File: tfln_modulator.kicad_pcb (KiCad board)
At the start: 4 copper layers, 60 x 40 mm, 9 parts

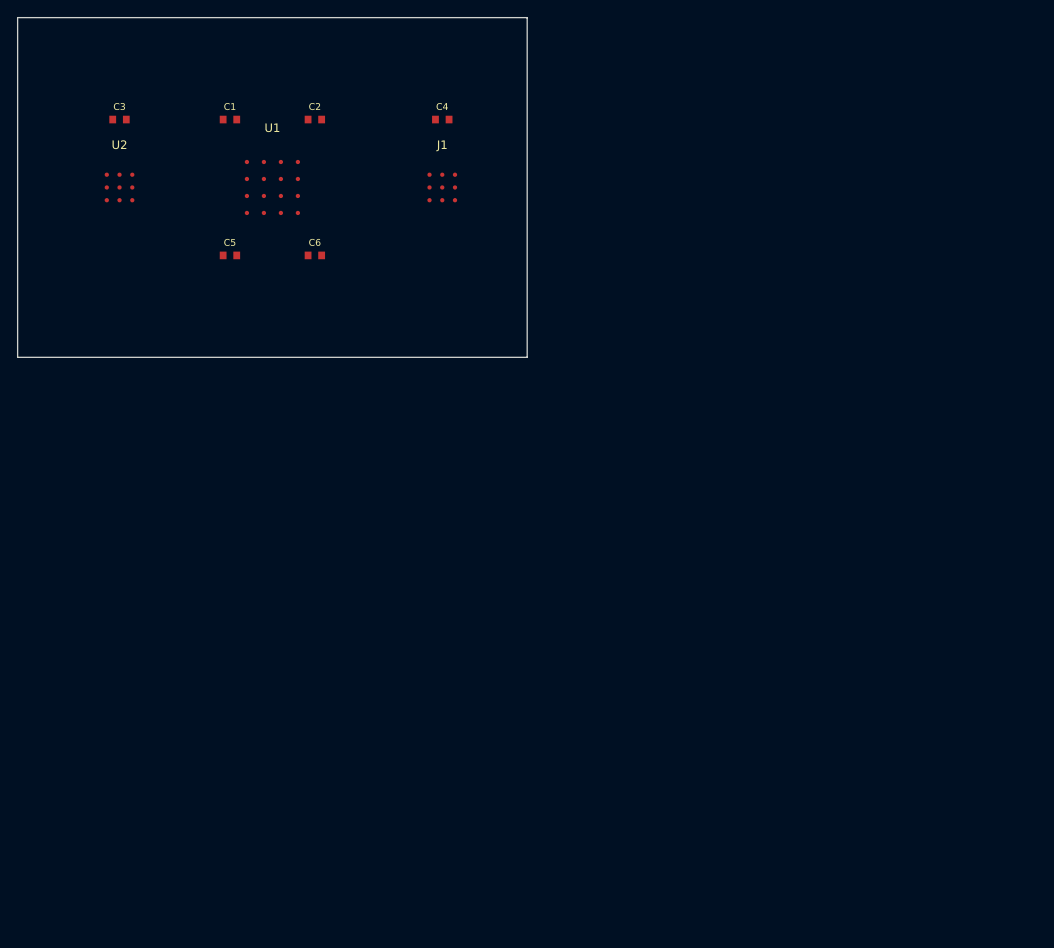
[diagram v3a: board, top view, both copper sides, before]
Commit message: Ultra high-density PCB: 634 nets, 600+ components, TFLN-AI Core + HBM + VRM
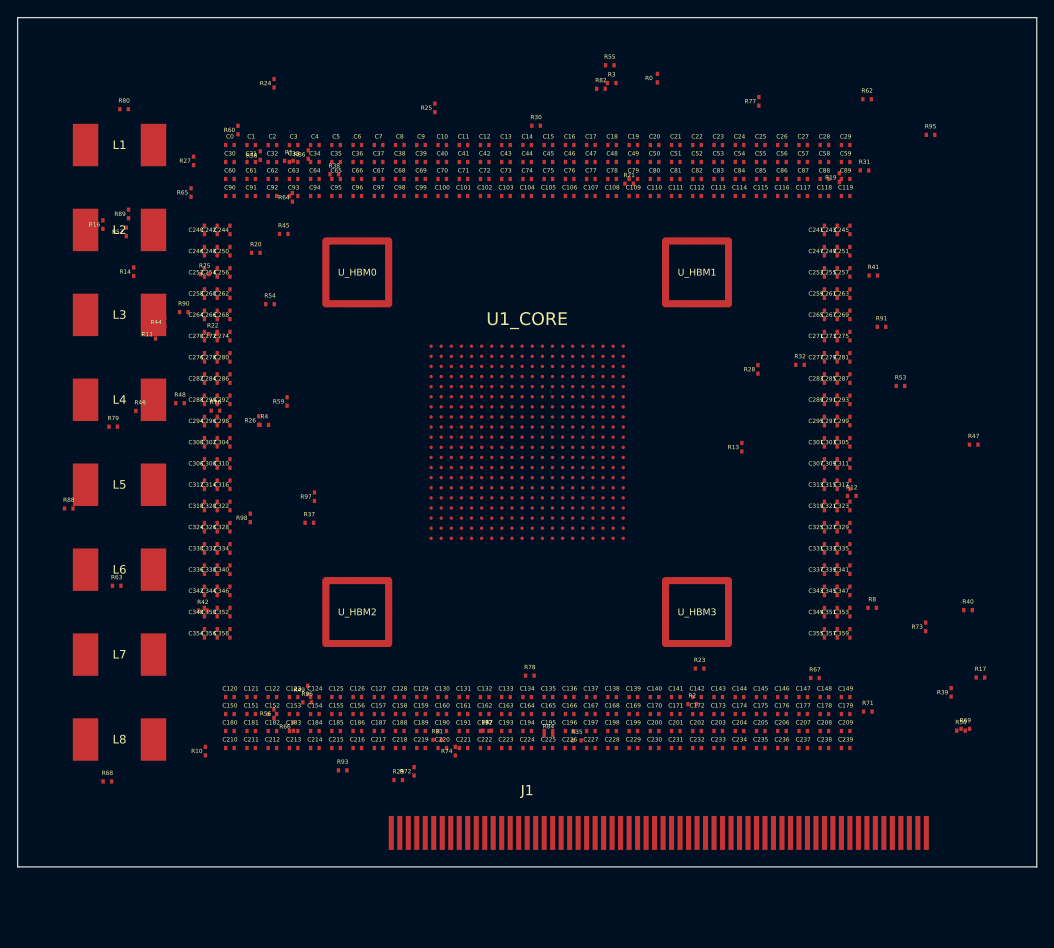
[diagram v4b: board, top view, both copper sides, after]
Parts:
- removed U1: , Custom:U1
- removed U2: , Custom:U2
- added C0: , SMD:0402, F.Cu at (25.0, 15.0)
- added C10: , SMD:0402, F.Cu at (50.0, 15.0)
- added C100: , SMD:0402, F.Cu at (50.0, 21.0)
- added C101: , SMD:0402, F.Cu at (52.5, 21.0)
- added C102: , SMD:0402, F.Cu at (55.0, 21.0)
- added C103: , SMD:0402, F.Cu at (57.5, 21.0)
- added C104: , SMD:0402, F.Cu at (60.0, 21.0)
- added C105: , SMD:0402, F.Cu at (62.5, 21.0)
- added C106: , SMD:0402, F.Cu at (65.0, 21.0)
- added C107: , SMD:0402, F.Cu at (67.5, 21.0)
- added C108: , SMD:0402, F.Cu at (70.0, 21.0)
- added C109: , SMD:0402, F.Cu at (72.5, 21.0)
- added C11: , SMD:0402, F.Cu at (52.5, 15.0)
- added C110: , SMD:0402, F.Cu at (75.0, 21.0)
- added C111: , SMD:0402, F.Cu at (77.5, 21.0)
- added C112: , SMD:0402, F.Cu at (80.0, 21.0)
- added C113: , SMD:0402, F.Cu at (82.5, 21.0)
- added C114: , SMD:0402, F.Cu at (85.0, 21.0)
- added C115: , SMD:0402, F.Cu at (87.5, 21.0)
- added C116: , SMD:0402, F.Cu at (90.0, 21.0)
- added C117: , SMD:0402, F.Cu at (92.5, 21.0)
- added C118: , SMD:0402, F.Cu at (95.0, 21.0)
- added C119: , SMD:0402, F.Cu at (97.5, 21.0)
- added C12: , SMD:0402, F.Cu at (55.0, 15.0)
- added C120: , SMD:0402, F.Cu at (25.0, 80.0)
- added C121: , SMD:0402, F.Cu at (27.5, 80.0)
- added C122: , SMD:0402, F.Cu at (30.0, 80.0)
- added C123: , SMD:0402, F.Cu at (32.5, 80.0)
- added C124: , SMD:0402, F.Cu at (35.0, 80.0)
- added C125: , SMD:0402, F.Cu at (37.5, 80.0)
- added C126: , SMD:0402, F.Cu at (40.0, 80.0)
- added C127: , SMD:0402, F.Cu at (42.5, 80.0)
- added C128: , SMD:0402, F.Cu at (45.0, 80.0)
- added C129: , SMD:0402, F.Cu at (47.5, 80.0)
- added C13: , SMD:0402, F.Cu at (57.5, 15.0)
- added C130: , SMD:0402, F.Cu at (50.0, 80.0)
- added C131: , SMD:0402, F.Cu at (52.5, 80.0)
- added C132: , SMD:0402, F.Cu at (55.0, 80.0)
- added C133: , SMD:0402, F.Cu at (57.5, 80.0)
- added C134: , SMD:0402, F.Cu at (60.0, 80.0)
- added C135: , SMD:0402, F.Cu at (62.5, 80.0)
- added C136: , SMD:0402, F.Cu at (65.0, 80.0)
- added C137: , SMD:0402, F.Cu at (67.5, 80.0)
- added C138: , SMD:0402, F.Cu at (70.0, 80.0)
- added C139: , SMD:0402, F.Cu at (72.5, 80.0)
- added C14: , SMD:0402, F.Cu at (60.0, 15.0)
- added C140: , SMD:0402, F.Cu at (75.0, 80.0)
- added C141: , SMD:0402, F.Cu at (77.5, 80.0)
- added C142: , SMD:0402, F.Cu at (80.0, 80.0)
- added C143: , SMD:0402, F.Cu at (82.5, 80.0)
- added C144: , SMD:0402, F.Cu at (85.0, 80.0)
- added C145: , SMD:0402, F.Cu at (87.5, 80.0)
- added C146: , SMD:0402, F.Cu at (90.0, 80.0)
- added C147: , SMD:0402, F.Cu at (92.5, 80.0)
- added C148: , SMD:0402, F.Cu at (95.0, 80.0)
- added C149: , SMD:0402, F.Cu at (97.5, 80.0)
- added C15: , SMD:0402, F.Cu at (62.5, 15.0)
- added C150: , SMD:0402, F.Cu at (25.0, 82.0)
- added C151: , SMD:0402, F.Cu at (27.5, 82.0)
- added C152: , SMD:0402, F.Cu at (30.0, 82.0)
- added C153: , SMD:0402, F.Cu at (32.5, 82.0)
- added C154: , SMD:0402, F.Cu at (35.0, 82.0)
- added C155: , SMD:0402, F.Cu at (37.5, 82.0)
- added C156: , SMD:0402, F.Cu at (40.0, 82.0)
- added C157: , SMD:0402, F.Cu at (42.5, 82.0)
- added C158: , SMD:0402, F.Cu at (45.0, 82.0)
- added C159: , SMD:0402, F.Cu at (47.5, 82.0)
- added C16: , SMD:0402, F.Cu at (65.0, 15.0)
- added C160: , SMD:0402, F.Cu at (50.0, 82.0)
- added C161: , SMD:0402, F.Cu at (52.5, 82.0)
- added C162: , SMD:0402, F.Cu at (55.0, 82.0)
- added C163: , SMD:0402, F.Cu at (57.5, 82.0)
- added C164: , SMD:0402, F.Cu at (60.0, 82.0)
- added C165: , SMD:0402, F.Cu at (62.5, 82.0)
- added C166: , SMD:0402, F.Cu at (65.0, 82.0)
- added C167: , SMD:0402, F.Cu at (67.5, 82.0)
- added C168: , SMD:0402, F.Cu at (70.0, 82.0)
- added C169: , SMD:0402, F.Cu at (72.5, 82.0)
- added C17: , SMD:0402, F.Cu at (67.5, 15.0)
- added C170: , SMD:0402, F.Cu at (75.0, 82.0)
- added C171: , SMD:0402, F.Cu at (77.5, 82.0)
- added C172: , SMD:0402, F.Cu at (80.0, 82.0)
- added C173: , SMD:0402, F.Cu at (82.5, 82.0)
- added C174: , SMD:0402, F.Cu at (85.0, 82.0)
- added C175: , SMD:0402, F.Cu at (87.5, 82.0)
- added C176: , SMD:0402, F.Cu at (90.0, 82.0)
- added C177: , SMD:0402, F.Cu at (92.5, 82.0)
- added C178: , SMD:0402, F.Cu at (95.0, 82.0)
- added C179: , SMD:0402, F.Cu at (97.5, 82.0)
- added C18: , SMD:0402, F.Cu at (70.0, 15.0)
- added C180: , SMD:0402, F.Cu at (25.0, 84.0)
- added C181: , SMD:0402, F.Cu at (27.5, 84.0)
- added C182: , SMD:0402, F.Cu at (30.0, 84.0)
- added C183: , SMD:0402, F.Cu at (32.5, 84.0)
- added C184: , SMD:0402, F.Cu at (35.0, 84.0)
- added C185: , SMD:0402, F.Cu at (37.5, 84.0)
- added C186: , SMD:0402, F.Cu at (40.0, 84.0)
- added C187: , SMD:0402, F.Cu at (42.5, 84.0)
- added C188: , SMD:0402, F.Cu at (45.0, 84.0)
- added C189: , SMD:0402, F.Cu at (47.5, 84.0)
- added C19: , SMD:0402, F.Cu at (72.5, 15.0)
- added C190: , SMD:0402, F.Cu at (50.0, 84.0)
- added C191: , SMD:0402, F.Cu at (52.5, 84.0)
- added C192: , SMD:0402, F.Cu at (55.0, 84.0)
- added C193: , SMD:0402, F.Cu at (57.5, 84.0)
- added C194: , SMD:0402, F.Cu at (60.0, 84.0)
- added C195: , SMD:0402, F.Cu at (62.5, 84.0)
- added C196: , SMD:0402, F.Cu at (65.0, 84.0)
- added C197: , SMD:0402, F.Cu at (67.5, 84.0)
- added C198: , SMD:0402, F.Cu at (70.0, 84.0)
- added C199: , SMD:0402, F.Cu at (72.5, 84.0)
- added C20: , SMD:0402, F.Cu at (75.0, 15.0)
- added C200: , SMD:0402, F.Cu at (75.0, 84.0)
- added C201: , SMD:0402, F.Cu at (77.5, 84.0)
- added C202: , SMD:0402, F.Cu at (80.0, 84.0)
- added C203: , SMD:0402, F.Cu at (82.5, 84.0)
- added C204: , SMD:0402, F.Cu at (85.0, 84.0)
- added C205: , SMD:0402, F.Cu at (87.5, 84.0)
- added C206: , SMD:0402, F.Cu at (90.0, 84.0)
- added C207: , SMD:0402, F.Cu at (92.5, 84.0)
- added C208: , SMD:0402, F.Cu at (95.0, 84.0)
- added C209: , SMD:0402, F.Cu at (97.5, 84.0)
- added C21: , SMD:0402, F.Cu at (77.5, 15.0)
- added C210: , SMD:0402, F.Cu at (25.0, 86.0)
- added C211: , SMD:0402, F.Cu at (27.5, 86.0)
- added C212: , SMD:0402, F.Cu at (30.0, 86.0)
- added C213: , SMD:0402, F.Cu at (32.5, 86.0)
- added C214: , SMD:0402, F.Cu at (35.0, 86.0)
- added C215: , SMD:0402, F.Cu at (37.5, 86.0)
- added C216: , SMD:0402, F.Cu at (40.0, 86.0)
- added C217: , SMD:0402, F.Cu at (42.5, 86.0)
- added C218: , SMD:0402, F.Cu at (45.0, 86.0)
- added C219: , SMD:0402, F.Cu at (47.5, 86.0)
- added C22: , SMD:0402, F.Cu at (80.0, 15.0)
- added C220: , SMD:0402, F.Cu at (50.0, 86.0)
- added C221: , SMD:0402, F.Cu at (52.5, 86.0)
- added C222: , SMD:0402, F.Cu at (55.0, 86.0)
- added C223: , SMD:0402, F.Cu at (57.5, 86.0)
- added C224: , SMD:0402, F.Cu at (60.0, 86.0)
- added C225: , SMD:0402, F.Cu at (62.5, 86.0)
- added C226: , SMD:0402, F.Cu at (65.0, 86.0)
- added C227: , SMD:0402, F.Cu at (67.5, 86.0)
- added C228: , SMD:0402, F.Cu at (70.0, 86.0)
- added C229: , SMD:0402, F.Cu at (72.5, 86.0)
- added C23: , SMD:0402, F.Cu at (82.5, 15.0)
- added C230: , SMD:0402, F.Cu at (75.0, 86.0)
- added C231: , SMD:0402, F.Cu at (77.5, 86.0)
- added C232: , SMD:0402, F.Cu at (80.0, 86.0)
- added C233: , SMD:0402, F.Cu at (82.5, 86.0)
- added C234: , SMD:0402, F.Cu at (85.0, 86.0)
- added C235: , SMD:0402, F.Cu at (87.5, 86.0)
- added C236: , SMD:0402, F.Cu at (90.0, 86.0)
- added C237: , SMD:0402, F.Cu at (92.5, 86.0)
- added C238: , SMD:0402, F.Cu at (95.0, 86.0)
- added C239: , SMD:0402, F.Cu at (97.5, 86.0)
- added C24: , SMD:0402, F.Cu at (85.0, 15.0)
- added C240: , SMD:0402, F.Cu at (22.0, 25.0)
- added C241: , SMD:0402, F.Cu at (95.0, 25.0)
- added C242: , SMD:0402, F.Cu at (23.5, 25.0)
- added C243: , SMD:0402, F.Cu at (96.5, 25.0)
- added C244: , SMD:0402, F.Cu at (25.0, 25.0)
- added C245: , SMD:0402, F.Cu at (98.0, 25.0)
- added C246: , SMD:0402, F.Cu at (22.0, 27.5)
- added C247: , SMD:0402, F.Cu at (95.0, 27.5)
- added C248: , SMD:0402, F.Cu at (23.5, 27.5)
- added C249: , SMD:0402, F.Cu at (96.5, 27.5)
- added C25: , SMD:0402, F.Cu at (87.5, 15.0)
- added C250: , SMD:0402, F.Cu at (25.0, 27.5)
- added C251: , SMD:0402, F.Cu at (98.0, 27.5)
- added C252: , SMD:0402, F.Cu at (22.0, 30.0)
- added C253: , SMD:0402, F.Cu at (95.0, 30.0)
- added C254: , SMD:0402, F.Cu at (23.5, 30.0)
- added C255: , SMD:0402, F.Cu at (96.5, 30.0)
- added C256: , SMD:0402, F.Cu at (25.0, 30.0)
- added C257: , SMD:0402, F.Cu at (98.0, 30.0)
- added C258: , SMD:0402, F.Cu at (22.0, 32.5)
- added C259: , SMD:0402, F.Cu at (95.0, 32.5)
- added C26: , SMD:0402, F.Cu at (90.0, 15.0)
- added C260: , SMD:0402, F.Cu at (23.5, 32.5)
- added C261: , SMD:0402, F.Cu at (96.5, 32.5)
- added C262: , SMD:0402, F.Cu at (25.0, 32.5)
- added C263: , SMD:0402, F.Cu at (98.0, 32.5)
- added C264: , SMD:0402, F.Cu at (22.0, 35.0)
- added C265: , SMD:0402, F.Cu at (95.0, 35.0)
- added C266: , SMD:0402, F.Cu at (23.5, 35.0)
- added C267: , SMD:0402, F.Cu at (96.5, 35.0)
- added C268: , SMD:0402, F.Cu at (25.0, 35.0)
- added C269: , SMD:0402, F.Cu at (98.0, 35.0)
- added C27: , SMD:0402, F.Cu at (92.5, 15.0)
- added C270: , SMD:0402, F.Cu at (22.0, 37.5)
- added C271: , SMD:0402, F.Cu at (95.0, 37.5)
- added C272: , SMD:0402, F.Cu at (23.5, 37.5)
- added C273: , SMD:0402, F.Cu at (96.5, 37.5)
- added C274: , SMD:0402, F.Cu at (25.0, 37.5)
- added C275: , SMD:0402, F.Cu at (98.0, 37.5)
- added C276: , SMD:0402, F.Cu at (22.0, 40.0)
- added C277: , SMD:0402, F.Cu at (95.0, 40.0)
- added C278: , SMD:0402, F.Cu at (23.5, 40.0)
- added C279: , SMD:0402, F.Cu at (96.5, 40.0)
- added C28: , SMD:0402, F.Cu at (95.0, 15.0)
- added C280: , SMD:0402, F.Cu at (25.0, 40.0)
- added C281: , SMD:0402, F.Cu at (98.0, 40.0)
- added C282: , SMD:0402, F.Cu at (22.0, 42.5)
- added C283: , SMD:0402, F.Cu at (95.0, 42.5)
- added C284: , SMD:0402, F.Cu at (23.5, 42.5)
- added C285: , SMD:0402, F.Cu at (96.5, 42.5)
- added C286: , SMD:0402, F.Cu at (25.0, 42.5)
- added C287: , SMD:0402, F.Cu at (98.0, 42.5)
- added C288: , SMD:0402, F.Cu at (22.0, 45.0)
- added C289: , SMD:0402, F.Cu at (95.0, 45.0)
- added C29: , SMD:0402, F.Cu at (97.5, 15.0)
- added C290: , SMD:0402, F.Cu at (23.5, 45.0)
- added C291: , SMD:0402, F.Cu at (96.5, 45.0)
- added C292: , SMD:0402, F.Cu at (25.0, 45.0)
- added C293: , SMD:0402, F.Cu at (98.0, 45.0)
- added C294: , SMD:0402, F.Cu at (22.0, 47.5)
- added C295: , SMD:0402, F.Cu at (95.0, 47.5)
- added C296: , SMD:0402, F.Cu at (23.5, 47.5)
- added C297: , SMD:0402, F.Cu at (96.5, 47.5)
- added C298: , SMD:0402, F.Cu at (25.0, 47.5)
- added C299: , SMD:0402, F.Cu at (98.0, 47.5)
- added C30: , SMD:0402, F.Cu at (25.0, 17.0)
- added C300: , SMD:0402, F.Cu at (22.0, 50.0)
- added C301: , SMD:0402, F.Cu at (95.0, 50.0)
- added C302: , SMD:0402, F.Cu at (23.5, 50.0)
- added C303: , SMD:0402, F.Cu at (96.5, 50.0)
- added C304: , SMD:0402, F.Cu at (25.0, 50.0)
- added C305: , SMD:0402, F.Cu at (98.0, 50.0)
- added C306: , SMD:0402, F.Cu at (22.0, 52.5)
- added C307: , SMD:0402, F.Cu at (95.0, 52.5)
- added C308: , SMD:0402, F.Cu at (23.5, 52.5)
- added C309: , SMD:0402, F.Cu at (96.5, 52.5)
- added C31: , SMD:0402, F.Cu at (27.5, 17.0)
- added C310: , SMD:0402, F.Cu at (25.0, 52.5)
- added C311: , SMD:0402, F.Cu at (98.0, 52.5)
- added C312: , SMD:0402, F.Cu at (22.0, 55.0)
- added C313: , SMD:0402, F.Cu at (95.0, 55.0)
- added C314: , SMD:0402, F.Cu at (23.5, 55.0)
- added C315: , SMD:0402, F.Cu at (96.5, 55.0)
- added C316: , SMD:0402, F.Cu at (25.0, 55.0)
- added C317: , SMD:0402, F.Cu at (98.0, 55.0)
- added C318: , SMD:0402, F.Cu at (22.0, 57.5)
- added C319: , SMD:0402, F.Cu at (95.0, 57.5)
- added C32: , SMD:0402, F.Cu at (30.0, 17.0)
- added C320: , SMD:0402, F.Cu at (23.5, 57.5)
- added C321: , SMD:0402, F.Cu at (96.5, 57.5)
- added C322: , SMD:0402, F.Cu at (25.0, 57.5)
- added C323: , SMD:0402, F.Cu at (98.0, 57.5)
- added C324: , SMD:0402, F.Cu at (22.0, 60.0)
- added C325: , SMD:0402, F.Cu at (95.0, 60.0)
- added C326: , SMD:0402, F.Cu at (23.5, 60.0)
- added C327: , SMD:0402, F.Cu at (96.5, 60.0)
- added C328: , SMD:0402, F.Cu at (25.0, 60.0)
- added C329: , SMD:0402, F.Cu at (98.0, 60.0)
- added C33: , SMD:0402, F.Cu at (32.5, 17.0)
- added C330: , SMD:0402, F.Cu at (22.0, 62.5)
- added C331: , SMD:0402, F.Cu at (95.0, 62.5)
- added C332: , SMD:0402, F.Cu at (23.5, 62.5)
- added C333: , SMD:0402, F.Cu at (96.5, 62.5)
- added C334: , SMD:0402, F.Cu at (25.0, 62.5)
- added C335: , SMD:0402, F.Cu at (98.0, 62.5)
- added C336: , SMD:0402, F.Cu at (22.0, 65.0)
- added C337: , SMD:0402, F.Cu at (95.0, 65.0)
- added C338: , SMD:0402, F.Cu at (23.5, 65.0)
- added C339: , SMD:0402, F.Cu at (96.5, 65.0)
- added C34: , SMD:0402, F.Cu at (35.0, 17.0)
- added C340: , SMD:0402, F.Cu at (25.0, 65.0)
- added C341: , SMD:0402, F.Cu at (98.0, 65.0)
- added C342: , SMD:0402, F.Cu at (22.0, 67.5)
- added C343: , SMD:0402, F.Cu at (95.0, 67.5)
- added C344: , SMD:0402, F.Cu at (23.5, 67.5)
- added C345: , SMD:0402, F.Cu at (96.5, 67.5)
- added C346: , SMD:0402, F.Cu at (25.0, 67.5)
- added C347: , SMD:0402, F.Cu at (98.0, 67.5)
- added C348: , SMD:0402, F.Cu at (22.0, 70.0)
- added C349: , SMD:0402, F.Cu at (95.0, 70.0)
- added C35: , SMD:0402, F.Cu at (37.5, 17.0)
- added C350: , SMD:0402, F.Cu at (23.5, 70.0)
- added C351: , SMD:0402, F.Cu at (96.5, 70.0)
- added C352: , SMD:0402, F.Cu at (25.0, 70.0)
- added C353: , SMD:0402, F.Cu at (98.0, 70.0)
- added C354: , SMD:0402, F.Cu at (22.0, 72.5)
- added C355: , SMD:0402, F.Cu at (95.0, 72.5)
- added C356: , SMD:0402, F.Cu at (23.5, 72.5)
- added C357: , SMD:0402, F.Cu at (96.5, 72.5)
- added C358: , SMD:0402, F.Cu at (25.0, 72.5)
- added C359: , SMD:0402, F.Cu at (98.0, 72.5)
- added C36: , SMD:0402, F.Cu at (40.0, 17.0)
- added C37: , SMD:0402, F.Cu at (42.5, 17.0)
- added C38: , SMD:0402, F.Cu at (45.0, 17.0)
- added C39: , SMD:0402, F.Cu at (47.5, 17.0)
- added C40: , SMD:0402, F.Cu at (50.0, 17.0)
- added C41: , SMD:0402, F.Cu at (52.5, 17.0)
- added C42: , SMD:0402, F.Cu at (55.0, 17.0)
- added C43: , SMD:0402, F.Cu at (57.5, 17.0)
- added C44: , SMD:0402, F.Cu at (60.0, 17.0)
- added C45: , SMD:0402, F.Cu at (62.5, 17.0)
- added C46: , SMD:0402, F.Cu at (65.0, 17.0)
- added C47: , SMD:0402, F.Cu at (67.5, 17.0)
- added C48: , SMD:0402, F.Cu at (70.0, 17.0)
- added C49: , SMD:0402, F.Cu at (72.5, 17.0)
- added C50: , SMD:0402, F.Cu at (75.0, 17.0)
- added C51: , SMD:0402, F.Cu at (77.5, 17.0)
- added C52: , SMD:0402, F.Cu at (80.0, 17.0)
- added C53: , SMD:0402, F.Cu at (82.5, 17.0)
- added C54: , SMD:0402, F.Cu at (85.0, 17.0)
- added C55: , SMD:0402, F.Cu at (87.5, 17.0)
- added C56: , SMD:0402, F.Cu at (90.0, 17.0)
- added C57: , SMD:0402, F.Cu at (92.5, 17.0)
- added C58: , SMD:0402, F.Cu at (95.0, 17.0)
- added C59: , SMD:0402, F.Cu at (97.5, 17.0)
- added C60: , SMD:0402, F.Cu at (25.0, 19.0)
- added C61: , SMD:0402, F.Cu at (27.5, 19.0)
- added C62: , SMD:0402, F.Cu at (30.0, 19.0)
- added C63: , SMD:0402, F.Cu at (32.5, 19.0)
- added C64: , SMD:0402, F.Cu at (35.0, 19.0)
- added C65: , SMD:0402, F.Cu at (37.5, 19.0)
- added C66: , SMD:0402, F.Cu at (40.0, 19.0)
- added C67: , SMD:0402, F.Cu at (42.5, 19.0)
- added C68: , SMD:0402, F.Cu at (45.0, 19.0)
- added C69: , SMD:0402, F.Cu at (47.5, 19.0)
- added C7: , SMD:0402, F.Cu at (42.5, 15.0)
- added C70: , SMD:0402, F.Cu at (50.0, 19.0)
- added C71: , SMD:0402, F.Cu at (52.5, 19.0)
- added C72: , SMD:0402, F.Cu at (55.0, 19.0)
- added C73: , SMD:0402, F.Cu at (57.5, 19.0)
- added C74: , SMD:0402, F.Cu at (60.0, 19.0)
- added C75: , SMD:0402, F.Cu at (62.5, 19.0)
- added C76: , SMD:0402, F.Cu at (65.0, 19.0)
- added C77: , SMD:0402, F.Cu at (67.5, 19.0)
- added C78: , SMD:0402, F.Cu at (70.0, 19.0)
- added C79: , SMD:0402, F.Cu at (72.5, 19.0)
- added C8: , SMD:0402, F.Cu at (45.0, 15.0)
- added C80: , SMD:0402, F.Cu at (75.0, 19.0)
- added C81: , SMD:0402, F.Cu at (77.5, 19.0)
- added C82: , SMD:0402, F.Cu at (80.0, 19.0)
- added C83: , SMD:0402, F.Cu at (82.5, 19.0)
- added C84: , SMD:0402, F.Cu at (85.0, 19.0)
- added C85: , SMD:0402, F.Cu at (87.5, 19.0)
- added C86: , SMD:0402, F.Cu at (90.0, 19.0)
- added C87: , SMD:0402, F.Cu at (92.5, 19.0)
- added C88: , SMD:0402, F.Cu at (95.0, 19.0)
- added C89: , SMD:0402, F.Cu at (97.5, 19.0)
- added C9: , SMD:0402, F.Cu at (47.5, 15.0)
- added C90: , SMD:0402, F.Cu at (25.0, 21.0)
- added C91: , SMD:0402, F.Cu at (27.5, 21.0)
- added C92: , SMD:0402, F.Cu at (30.0, 21.0)
- added C93: , SMD:0402, F.Cu at (32.5, 21.0)
- added C94: , SMD:0402, F.Cu at (35.0, 21.0)
- added C95: , SMD:0402, F.Cu at (37.5, 21.0)
- added C96: , SMD:0402, F.Cu at (40.0, 21.0)
- added C97: , SMD:0402, F.Cu at (42.5, 21.0)
- added C98: , SMD:0402, F.Cu at (45.0, 21.0)
- added C99: , SMD:0402, F.Cu at (47.5, 21.0)
- added L1: , Inductor:L_1210, F.Cu at (12.0, 15.0)
- added L2: , Inductor:L_1210, F.Cu at (12.0, 25.0)
- added L3: , Inductor:L_1210, F.Cu at (12.0, 35.0)
- added L4: , Inductor:L_1210, F.Cu at (12.0, 45.0)
- added L5: , Inductor:L_1210, F.Cu at (12.0, 55.0)
- added L6: , Inductor:L_1210, F.Cu at (12.0, 65.0)
- added L7: , Inductor:L_1210, F.Cu at (12.0, 75.0)
- added L8: , Inductor:L_1210, F.Cu at (12.0, 85.0)
- added R0: , SMD:0402, F.Cu at (75.3, 7.13)
- added R1: , SMD:0402, F.Cu at (31.9, 16.9)
- added R10: , SMD:0402, F.Cu at (22.1, 86.4)
- added R11: , SMD:0402, F.Cu at (16.2, 37.3)
- added R12: , SMD:0402, F.Cu at (98.2, 56.3)
- added R13: , SMD:0402, F.Cu at (85.3, 50.6)
- added R14: , SMD:0402, F.Cu at (13.7, 29.9)
- added R16: , SMD:0402, F.Cu at (10.0, 24.4)
- added R17: , SMD:0402, F.Cu at (113.4, 77.7)
- added R19: , SMD:0402, F.Cu at (96.8, 18.8)
- added R2: , SMD:0402, F.Cu at (79.4, 80.8)
- added R20: , SMD:0402, F.Cu at (28.0, 27.7)
- added R21: , SMD:0402, F.Cu at (72.0, 19.5)
- added R22: , SMD:0402, F.Cu at (23.0, 37.3)
- added R23: , SMD:0402, F.Cu at (80.3, 76.6)
- added R24: , SMD:0402, F.Cu at (30.2, 7.73)
- added R25: , SMD:0402, F.Cu at (49.1, 10.6)
- added R26: , SMD:0402, F.Cu at (28.4, 47.4)
- added R27: , SMD:0402, F.Cu at (20.7, 16.9)
- added R28: , SMD:0402, F.Cu at (87.2, 41.4)
- added R29: , SMD:0402, F.Cu at (44.8, 89.8)
- added R3: , SMD:0402, F.Cu at (70.0, 7.70)
- added R30: , SMD:0402, F.Cu at (61.0, 12.7)
- added R31: , SMD:0402, F.Cu at (99.7, 18.0)
- added R32: , SMD:0402, F.Cu at (92.1, 40.9)
- added R35: , SMD:0402, F.Cu at (65.9, 85.1)
- added R37: , SMD:0402, F.Cu at (34.4, 59.5)
- added R38: , SMD:0402, F.Cu at (37.3, 18.4)
- added R39: , SMD:0402, F.Cu at (109.9, 79.4)
- added R4: , SMD:0402, F.Cu at (29.1, 48.0)
- added R40: , SMD:0402, F.Cu at (111.9, 69.8)
- added R41: , SMD:0402, F.Cu at (100.8, 30.4)
- added R42: , SMD:0402, F.Cu at (21.8, 69.8)
- added R44: , SMD:0402, F.Cu at (17.3, 35.9)
- added R45: , SMD:0402, F.Cu at (31.3, 25.5)
- added R46: , SMD:0402, F.Cu at (14.4, 46.3)
- added R47: , SMD:0402, F.Cu at (112.6, 50.3)
- added R48: , SMD:0402, F.Cu at (19.1, 45.4)
- added R49: , SMD:0402, F.Cu at (34.2, 79.2)
- added R50: , SMD:0402, F.Cu at (111.1, 84.0)
- added R53: , SMD:0402, F.Cu at (104.0, 43.4)
- added R54: , SMD:0402, F.Cu at (29.7, 33.7)
- added R55: , SMD:0402, F.Cu at (69.7, 5.61)
- added R56: , SMD:0402, F.Cu at (30.2, 82.0)
- added R57: , SMD:0402, F.Cu at (12.8, 25.2)
- added R58: , SMD:0402, F.Cu at (28.6, 16.2)
- added R59: , SMD:0402, F.Cu at (31.7, 45.2)
- added R60: , SMD:0402, F.Cu at (25.9, 13.2)
- added R62: , SMD:0402, F.Cu at (100.0, 9.60)
- added R63: , SMD:0402, F.Cu at (11.7, 66.9)
- added R64: , SMD:0402, F.Cu at (32.4, 21.2)
- added R65: , SMD:0402, F.Cu at (20.4, 20.6)
- added R66: , SMD:0402, F.Cu at (32.5, 83.5)
- added R67: , SMD:0402, F.Cu at (93.9, 77.8)
- added R68: , SMD:0402, F.Cu at (10.6, 89.9)
- added R69: , SMD:0402, F.Cu at (111.6, 83.7)
- added R70: , SMD:0402, F.Cu at (23.3, 46.3)
- added R71: , SMD:0402, F.Cu at (100.1, 81.7)
- added R72: , SMD:0402, F.Cu at (46.7, 88.8)
- added R73: , SMD:0402, F.Cu at (106.9, 71.7)
- added R74: , SMD:0402, F.Cu at (51.5, 86.4)
- added R75: , SMD:0402, F.Cu at (22.0, 30.2)
- added R77: , SMD:0402, F.Cu at (87.3, 9.86)
- added R78: , SMD:0402, F.Cu at (60.3, 77.5)
- added R79: , SMD:0402, F.Cu at (11.3, 48.2)
- added R8: , SMD:0402, F.Cu at (100.6, 69.5)
- added R80: , SMD:0402, F.Cu at (12.5, 10.8)
- added R81: , SMD:0402, F.Cu at (49.4, 85.0)
- added R82: , SMD:0402, F.Cu at (68.7, 8.38)
- added R84: , SMD:0402, F.Cu at (62.5, 84.5)
- added R86: , SMD:0402, F.Cu at (34.2, 16.1)
- added R87: , SMD:0402, F.Cu at (55.3, 84.0)
- added R88: , SMD:0402, F.Cu at (6.02, 57.8)
- added R89: , SMD:0402, F.Cu at (13.1, 23.1)
- added R90: , SMD:0402, F.Cu at (19.6, 34.7)
- added R91: , SMD:0402, F.Cu at (101.7, 36.4)
- added R93: , SMD:0402, F.Cu at (38.3, 88.6)
- added R95: , SMD:0402, F.Cu at (107.5, 13.8)
- added R96: , SMD:0402, F.Cu at (34.1, 80.6)
- added R97: , SMD:0402, F.Cu at (35.0, 56.4)
- added R98: , SMD:0402, F.Cu at (27.4, 58.9)
- added U1_CORE: , BGA:U1_CORE, F.Cu at (60.0, 50.0)
- added U_HBM0: , QFN:U_HBM0, F.Cu at (40.0, 30.0)
- added U_HBM1: , QFN:U_HBM1, F.Cu at (80.0, 30.0)
- added U_HBM2: , QFN:U_HBM2, F.Cu at (40.0, 70.0)
- added U_HBM3: , QFN:U_HBM3, F.Cu at (80.0, 70.0)
- C1, C2, C3, C4, C5, C6: footprint Capacitor_SMD:C_0603 -> SMD:0402
- J1: footprint Custom:J1 -> Connector:PCIe_x16
- moved J1 76.7 mm to (60.0, 96.0)
- moved C3 20.7 mm to (32.5, 15.0)
- moved C5 18.0 mm to (37.5, 15.0)
- moved C4 15.3 mm to (35.0, 15.0)
- moved C6 13.9 mm to (40.0, 15.0)
- moved C2 5.83 mm to (30.0, 15.0)
- moved C1 3.91 mm to (27.5, 15.0)
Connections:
- net SIG15 renamed PCIE1_RX_P
- net SIG16 renamed PCIE1_RX_N
- net SIG17 renamed PCIE2_TX_P
- C1 pad 1: VCC -> HBM0_D1
- C2 pad 1: +3V3 -> HBM0_D2
- C3 pad 1: VCC -> HBM0_D3
- C4 pad 1: VCC -> HBM0_D4
- C5 pad 1: SIG6 -> HBM0_D5
- C6 pad 1: SIG7 -> HBM0_D6
- J1 pad 1: SIG2 -> PCIE0_TX_P
- J1 pad 2: SIG3 -> PCIE0_TX_N
- J1 pad 3: SIG4 -> PCIE0_RX_P
- J1 pad 4: SIG5 -> PCIE0_RX_N
- J1 pad 5: GND -> PCIE1_TX_P
- J1 pad 6: VCC -> PCIE1_TX_N
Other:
- board size 60 x 40 mm -> 120 x 100 mm
